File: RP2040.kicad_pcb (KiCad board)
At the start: 4 copper layers, 15.2 x 30.5 mm, 32 parts, among them J1 USB_B_Micro, J2 Conn_01x12, J3 Conn_01x12, SW1 USB_BOOT, SW2 RESET, U1 AP1117-33, U2 W25Q128JVS, U3 RP2040, Y1 12MHz

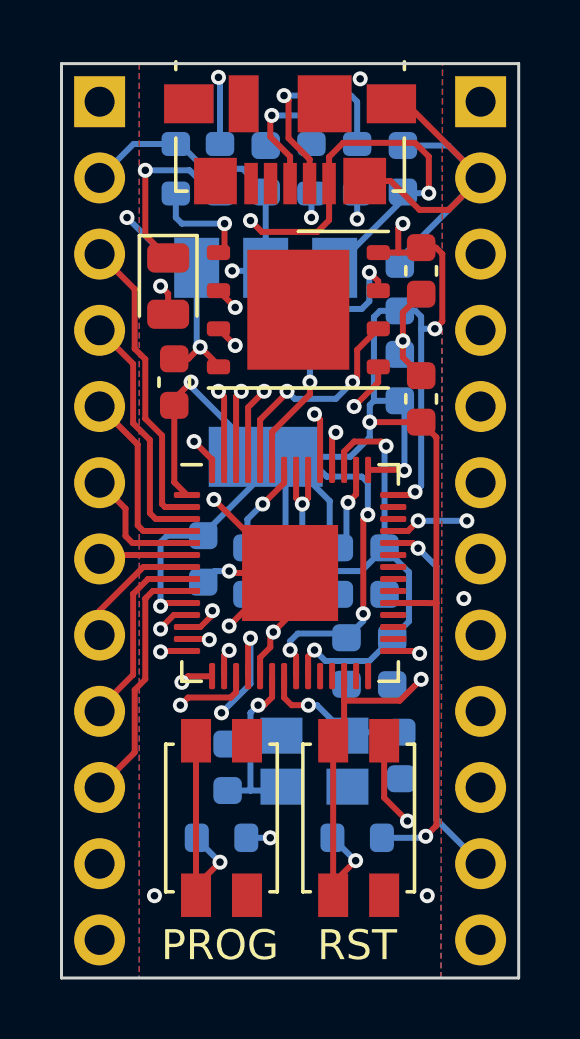
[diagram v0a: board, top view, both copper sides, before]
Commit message: fix: Fix crystal orientation
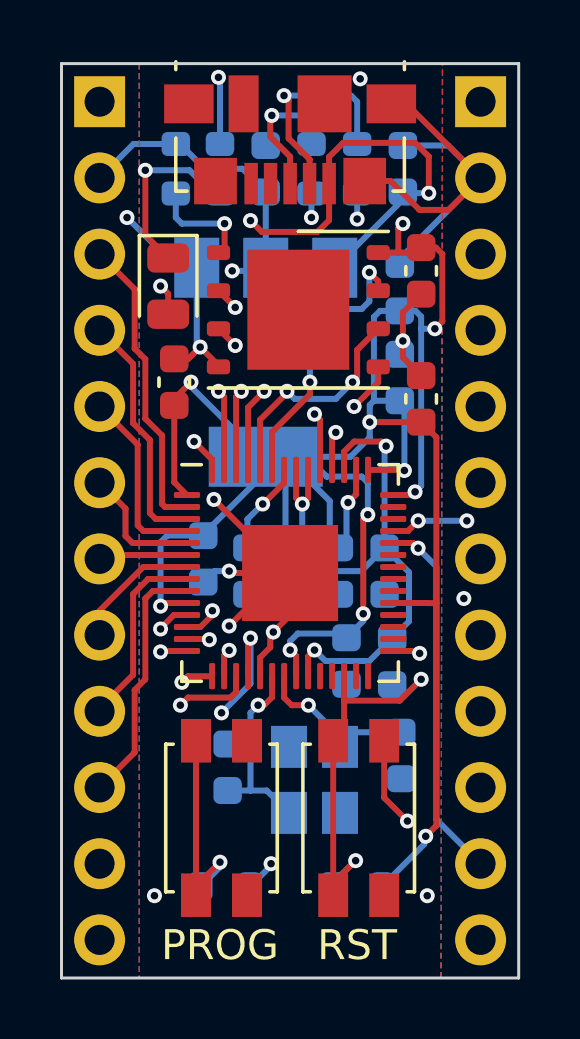
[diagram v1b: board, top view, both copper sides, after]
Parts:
- moved R1 1.63 mm to (110.9, 89.7)
- moved R3 1.63 mm to (115.3, 89.7)
- moved Y1 0.62 mm to (113.8, 86.1), turned to -90 degrees
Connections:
- Y1 pad 1: GND -> Net-(U3-XOUT)
- Y1 pad 2: Net-(U3-XIN) -> GND
- Y1 pad 3: GND -> Net-(U3-XIN)
- Y1 pad 4: Net-(U3-XOUT) -> GND
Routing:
- net +3V3: track 105.6 -> 106.4 mm
- net QSPI_SS: track 33.1 -> 33.8 mm
- net Net-(U3-XOUT): track 5.20 -> 5.78 mm
- net Net-(U3-XIN): track 6.08 -> 6.59 mm
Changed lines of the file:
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@@
 	(footprint "Resistor_SMD:R_0603_1608Metric"
 		(layer "B.Cu")
-		(at 110.744 88.0364 180)
+		(at 110.871 89.662 180)
 		(descr "Resistor SMD 0603 (1608 Metric), square (rectangular) end terminal, IPC_7351 nominal, (Body size source: IPC-SM-782 page 72, https://www.pcb-3d.com/wordpress/wp-content/uploads/ipc-sm-782a_amendment_1_and_2.pdf), generated with kicad-footprint-generator")
 		(tags "resistor")
@@
 	(footprint "Crystal:Crystal_SMD_3225-4Pin_3.2x2.5mm"
 		(layer "B.Cu")
-		(at 113.8428 85.4828 180)
+		(at 113.8428 86.106 -90)
 		(descr "SMD Crystal SERIES SMD3225/4 http://www.txccrystal.com/images/pdf/7m-accuracy.pdf, 3.2x2.5mm^2 package")
 		(tags "SMD SMT crystal")
 		(property "Reference" "Y1"
-			(at 0 2.45 0)
+			(at 0 2.45 90)
 			(layer "B.SilkS")
 			(hide yes)
@@
 		)
 		(property "Value" "12MHz"
-			(at 0 -2.45 0)
+			(at 0 -2.45 90)
 			(layer "B.Fab")
 			(hide yes)
@@
 		)
 		(property "Datasheet" ""
-			(at 0 0 180)
+			(at 0 0 90)
 			(layer "F.Fab")
 			(hide yes)
@@
 		)
 		(property "Description" ""
-			(at 0 0 180)
+			(at 0 0 90)
 			(layer "F.Fab")
 			(hide yes)
@@
 		)
 		(fp_line
-			(start 2.1 1.7)
-			(end -2.1 1.7)
+			(start -2.1 1.7)
+			(end -2.1 -1.7)
 			(stroke
 				(width 0.05)
@@
 		)
 		(fp_line
-			(start 2.1 -1.7)
-			(end 2.1 1.7)
+			(start 2.1 1.7)
+			(end -2.1 1.7)
 			(stroke
 				(width 0.05)
@@
 		)
 		(fp_line
-			(start -2.1 1.7)
-			(end -2.1 -1.7)
+			(start -2.1 -1.7)
+			(end 2.1 -1.7)
 			(stroke
 				(width 0.05)
@@
 		)
 		(fp_line
-			(start -2.1 -1.7)
-			(end 2.1 -1.7)
+			(start 2.1 -1.7)
+			(end 2.1 1.7)
 			(stroke
 				(width 0.05)
@@
 		)
 		(fp_line
-			(start 1.6 1.25)
-			(end -1.6 1.25)
+			(start -1.6 1.25)
+			(end -1.6 -1.25)
 			(stroke
 				(width 0.1)
@@
 		)
 		(fp_line
-			(start 1.6 -1.25)
-			(end 1.6 1.25)
+			(start 1.6 1.25)
+			(end -1.6 1.25)
 			(stroke
 				(width 0.1)
@@
 		)
 		(fp_line
-			(start -1.6 1.25)
-			(end -1.6 -1.25)
+			(start -1.6 -0.25)
+			(end -0.6 -1.25)
 			(stroke
 				(width 0.1)
@@
 		)
 		(fp_line
-			(start -1.6 -0.25)
-			(end -0.6 -1.25)
+			(start -1.6 -1.25)
+			(end 1.6 -1.25)
 			(stroke
 				(width 0.1)
@@
 		)
 		(fp_line
-			(start -1.6 -1.25)
-			(end 1.6 -1.25)
+			(start 1.6 -1.25)
+			(end 1.6 1.25)
 			(stroke
 				(width 0.1)
@@
 		)
 		(pad "1" smd rect
-			(at -1.1 -0.85 180)
+			(at -1.1 -0.85 270)
 			(size 1.4 1.2)
 			(layers "B.Cu" "B.Mask" "B.Paste")
-			(net "GND")
+			(net "Net-(U3-XOUT)")
 			(pinfunction "1_1")
 			(pintype "passive")
 		)
 		(pad "2" smd rect
-			(at 1.1 -0.85 180)
+			(at 1.1 -0.85 270)
 			(size 1.4 1.2)
 			(layers "B.Cu" "B.Mask" "B.Paste")
-			(net "Net-(U3-XIN)")
+			(net "GND")
 			(pinfunction "2_2")
 			(pintype "passive")
 		)
 		(pad "3" smd rect
-			(at 1.1 0.85 180)
+			(at 1.1 0.85 270)
 			(size 1.4 1.2)
 			(layers "B.Cu" "B.Mask" "B.Paste")
-			(net "GND")
+			(net "Net-(U3-XIN)")
 			(pinfunction "3_3")
 			(pintype "passive")
 		)
 		(pad "4" smd rect
-			(at -1.1 0.85 180)
+			(at -1.1 0.85 270)
 			(size 1.4 1.2)
 			(layers "B.Cu" "B.Mask" "B.Paste")
-			(net "Net-(U3-XOUT)")
+			(net "GND")
 			(pinfunction "4_4")
 			(pintype "passive")
@@
 	(footprint "Resistor_SMD:R_0603_1608Metric"
 		(layer "B.Cu")
-		(at 115.2652 88.0364 180)
+		(at 115.2652 89.662 180)
 		(descr "Resistor SMD 0603 (1608 Metric), square (rectangular) end terminal, IPC_7351 nominal, (Body size source: IPC-SM-782 page 72, https://www.pcb-3d.com/wordpress/wp-content/uploads/ipc-sm-782a_amendment_1_and_2.pdf), generated with kicad-footprint-generator")
 		(tags "resistor")
@@
 	)
 	(segment
+		(start 116.0902 89.662)
+		(end 117.5004 88.2518)
+		(width 0.2)
+		(layer "B.Cu")
+		(net "+3V3")
+	)
+	(segment
 		(start 110.1344 77.9272)
 		(end 112.2172 75.8444)
@@
 	)
 	(segment
-		(start 116.0902 88.0364)
-		(end 117.5004 88.0364)
-		(width 0.2)
-		(layer "B.Cu")
-		(net "+3V3")
-	)
-	(segment
 		(start 115.6846 74.6884)
 		(end 115.0366 75.3364)
@@
 	)
 	(segment
-		(start 117.5004 88.0364)
-		(end 117.5512 87.9856)
-		(width 0.2)
-		(layer "B.Cu")
-		(net "+3V3")
-	)
-	(segment
 		(start 114.3508 78.0666)
 		(end 114.6556 78.3714)
@@
 	)
 	(segment
+		(start 117.5004 88.2518)
+		(end 117.5004 88.0364)
+		(width 0.2)
+		(layer "B.Cu")
+		(net "+3V3")
+	)
+	(segment
+		(start 117.5004 88.0364)
+		(end 117.5512 87.9856)
+		(width 0.2)
+		(layer "B.Cu")
+		(net "+3V3")
+	)
+	(segment
 		(start 112.2172 75.8444)
 		(end 112.2172 75.3364)
@@
 	(segment
 		(start 111.7092 86.461)
-		(end 112.6146 86.461)
+		(end 112.2478 86.461)
 		(width 0.2)
 		(layer "B.Cu")
@@
 	)
 	(segment
-		(start 112.6146 86.461)
-		(end 112.7428 86.3328)
+		(start 111.9632 83.6168)
+		(end 111.7092 83.8708)
 		(width 0.2)
 		(layer "B.Cu")
@@
 	)
 	(segment
-		(start 111.9632 83.6168)
-		(end 111.7092 83.8708)
+		(start 112.2478 86.461)
+		(end 112.9928 87.206)
 		(width 0.2)
 		(layer "B.Cu")
@@
 	)
 	(segment
-		(start 113.9268 83.6168)
-		(end 114.9428 84.6328)
+		(start 113.6396 83.6168)
+		(end 114.6928 84.67)
 		(width 0.2)
 		(layer "B.Cu")
@@
 	)
 	(segment
-		(start 113.6396 83.6168)
-		(end 113.9268 83.6168)
+		(start 114.6928 84.67)
+		(end 114.6928 85.006)
+		(width 0.2)
+		(layer "B.Cu")
+		(net "Net-(U3-XOUT)")
+	)
+	(segment
+		(start 115.058 84.5176)
+		(end 116.7384 84.5176)
 		(width 0.2)
 		(layer "B.Cu")
@@
 	)
 	(segment
-		(start 116.7384 84.5176)
+		(start 114.6928 84.8828)
 		(end 115.058 84.5176)
 		(width 0.2)
@@
 	)
 	(segment
-		(start 115.058 84.5176)
-		(end 114.9428 84.6328)
+		(start 114.6928 85.006)
+		(end 114.6928 84.8828)
 		(width 0.2)
 		(layer "B.Cu")
@@
 	)
 	(segment
+		(start 114.4402 89.5604)
+		(end 114.4402 89.662)
+		(width 0.2)
+		(layer "B.Cu")
+		(net "~{Reset}")
+	)
+	(segment
 		(start 115.2022 88.7984)
-		(end 114.4402 88.0364)
+		(end 114.4402 89.5604)
 		(width 0.2)
 		(layer "B.Cu")
@@
 	)
 	(via
-		(at 112.3696 88.0364)
+		(at 112.395 88.9)
 		(size 0.5)
 		(drill 0.25)
@@
 	)
 	(segment
-		(start 110.8456 67.564)
-		(end 109.4232 67.564)
+		(start 112.395 88.9)
+		(end 112.395 88.963)
 		(width 0.2)
 		(layer "B.Cu")
@@
 	)
 	(segment
-		(start 112.3696 88.0364)
-		(end 111.569 88.0364)
+		(start 110.8456 67.564)
+		(end 109.4232 67.564)
 		(width 0.2)
 		(layer "B.Cu")
@@
 	)
 	(segment
+		(start 112.395 88.963)
+		(end 111.696 89.662)
+		(width 0.2)
+		(layer "B.Cu")
+		(net "QSPI_SS")
+	)
+	(segment
 		(start 109.22 67.3608)
 		(end 109.22 66.5602)
@@
 	)
 	(segment
-		(start 110.8456 67.564)
-		(end 108.5088 67.564)
+		(start 108.7628 82.6516)
+		(end 109.5248 81.8896)
 		(width 0.2)
 		(layer "In1.Cu")
@@
 	)
 	(segment
-		(start 109.8296 74.8284)
-		(end 109.5248 75.1332)
+		(start 112.395 88.9)
+		(end 111.5314 88.0364)
+		(width 0.2)
+		(layer "In1.Cu")
+		(net "QSPI_SS")
+	)
+	(segment
+		(start 110.8456 67.564)
+		(end 108.5088 67.564)
 		(width 0.2)
 		(layer "In1.Cu")
@@
 	)
 	(segment
-		(start 108.7628 82.6516)
-		(end 108.7628 87.884)
+		(start 108.7628 87.884)
+		(end 108.7628 82.6516)
 		(width 0.2)
 		(layer "In1.Cu")
@@
 	(segment
 		(start 108.9152 88.0364)
-		(end 112.3696 88.0364)
+		(end 108.7628 87.884)
 		(width 0.2)
 		(layer "In1.Cu")
@@
 	)
 	(segment
-		(start 109.5248 75.1332)
-		(end 109.5248 81.8896)
+		(start 111.5314 88.0364)
+		(end 108.9152 88.0364)
 		(width 0.2)
 		(layer "In1.Cu")
@@
 	)
 	(segment
-		(start 109.5248 81.8896)
-		(end 108.7628 82.6516)
+		(start 108.5088 67.564)
+		(end 108.204 67.8688)
 		(width 0.2)
 		(layer "In1.Cu")
@@
 	)
 	(segment
-		(start 108.7628 87.884)
-		(end 108.9152 88.0364)
+		(start 109.5248 81.8896)
+		(end 109.5248 75.1332)
 		(width 0.2)
 		(layer "In1.Cu")
@@
 	)
 	(segment
-		(start 108.5088 67.564)
-		(end 108.204 67.8688)
+		(start 109.5248 75.1332)
+		(end 109.8296 74.8284)
 		(width 0.2)
 		(layer "In1.Cu")
@@
 	(segment
 		(start 109.894 89.951)
-		(end 109.894 89.6484)
+		(end 109.894 84.801)
 		(width 0.2)
 		(layer "F.Cu")
@@
 	(segment
 		(start 109.894 89.6484)
-		(end 110.6932 88.8492)
+		(end 109.894 89.951)
 		(width 0.2)
 		(layer "F.Cu")
@@
 	)
 	(segment
-		(start 109.894 89.951)
-		(end 109.894 84.801)
+		(start 110.6932 88.8492)
+		(end 109.894 89.6484)
 		(width 0.2)
 		(layer "F.Cu")
@@
 	)
 	(segment
-		(start 109.919 88.075)
-		(end 110.6932 88.8492)
+		(start 110.6932 89.0148)
+		(end 110.046 89.662)
 		(width 0.2)
 		(layer "B.Cu")
@@
 	)
 	(segment
-		(start 109.919 88.0364)
-		(end 109.919 88.075)
+		(start 110.6932 88.8492)
+		(end 110.6932 89.0148)
 		(width 0.2)
 		(layer "B.Cu")
